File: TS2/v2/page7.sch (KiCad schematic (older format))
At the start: 9 parts, among them P1 FTDI (TERMINAL), P2 FTDI (HOST), U29 6850, U3 74LS00, U30 6850, U31 MC14411, U5 74LS04, Y1 1.842MHz

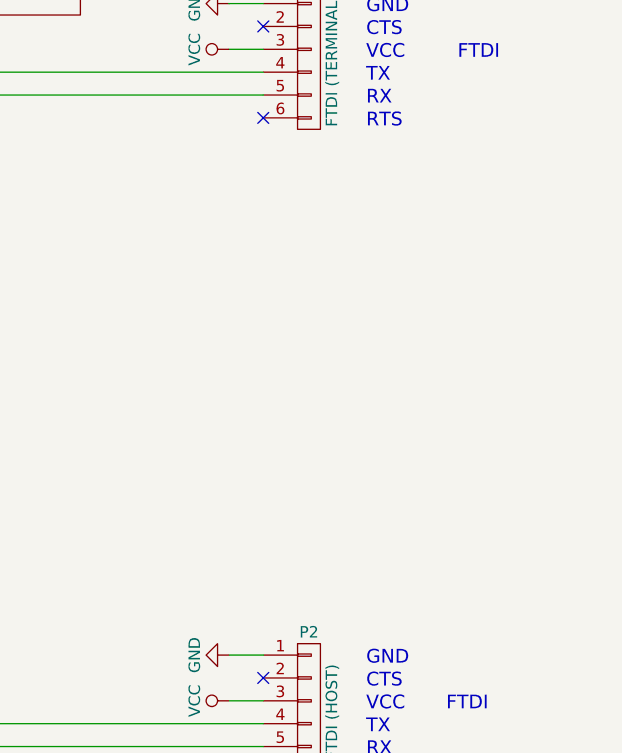
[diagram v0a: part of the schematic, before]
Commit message: Label serial ports.
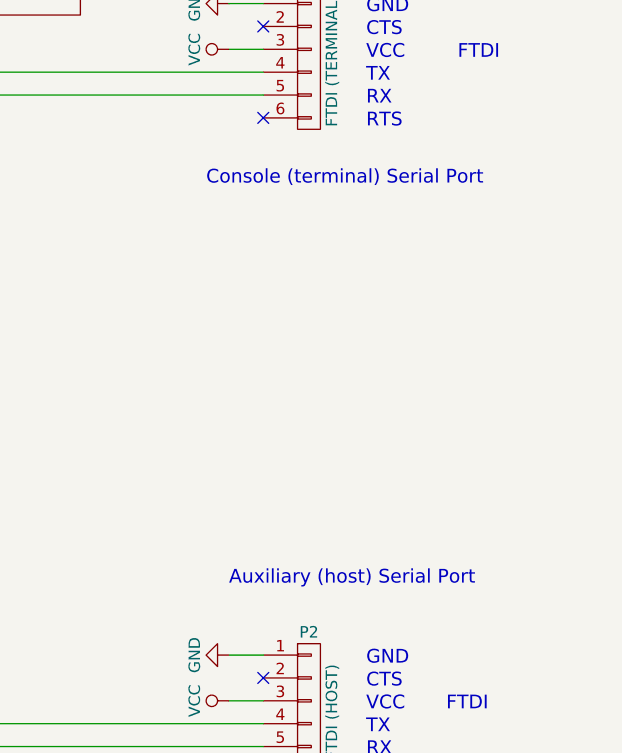
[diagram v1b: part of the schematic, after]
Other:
- note added: "Auxiliary (host) Serial Port"
- note added: "Console (terminal) Serial Port"
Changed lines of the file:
@@
 	2400 4050 2400 4250
 Connection ~ 2400 4150
+Text Notes 8450 4550 0    60   ~ 0
+Auxiliary (host) Serial Port
+Text Notes 8350 2800 0    60   ~ 0
+Console (terminal) Serial Port
 $EndSCHEMATC

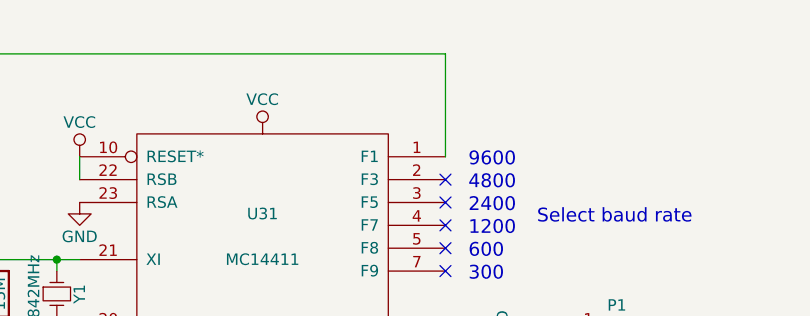
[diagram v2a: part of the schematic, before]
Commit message: List frequency of clock generator.
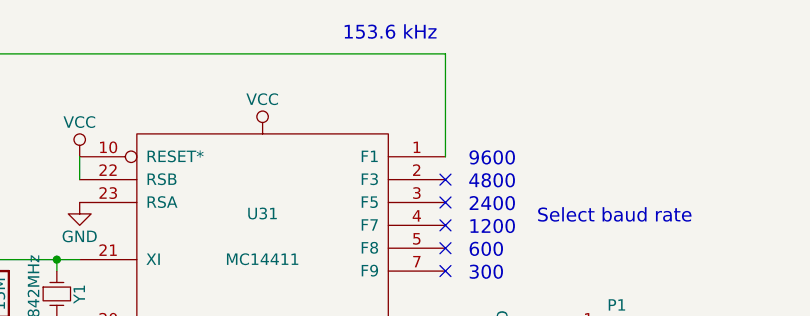
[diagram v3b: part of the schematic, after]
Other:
- note added: "153.6 kHz"
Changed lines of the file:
@@
 Text Notes 8350 2800 0    60   ~ 0
 Console (terminal) Serial Port
+Text Notes 7600 750  0    60   ~ 0
+153.6 kHz
 $EndSCHEMATC

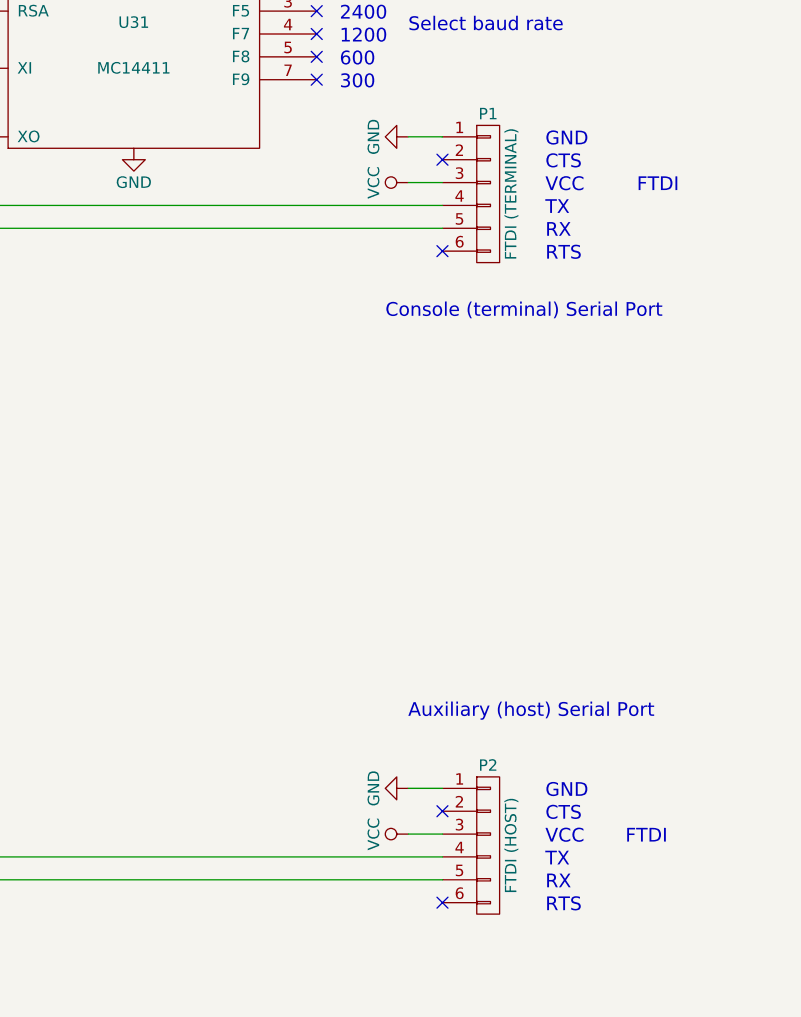
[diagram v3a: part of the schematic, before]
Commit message: Correction to FTDI connections.
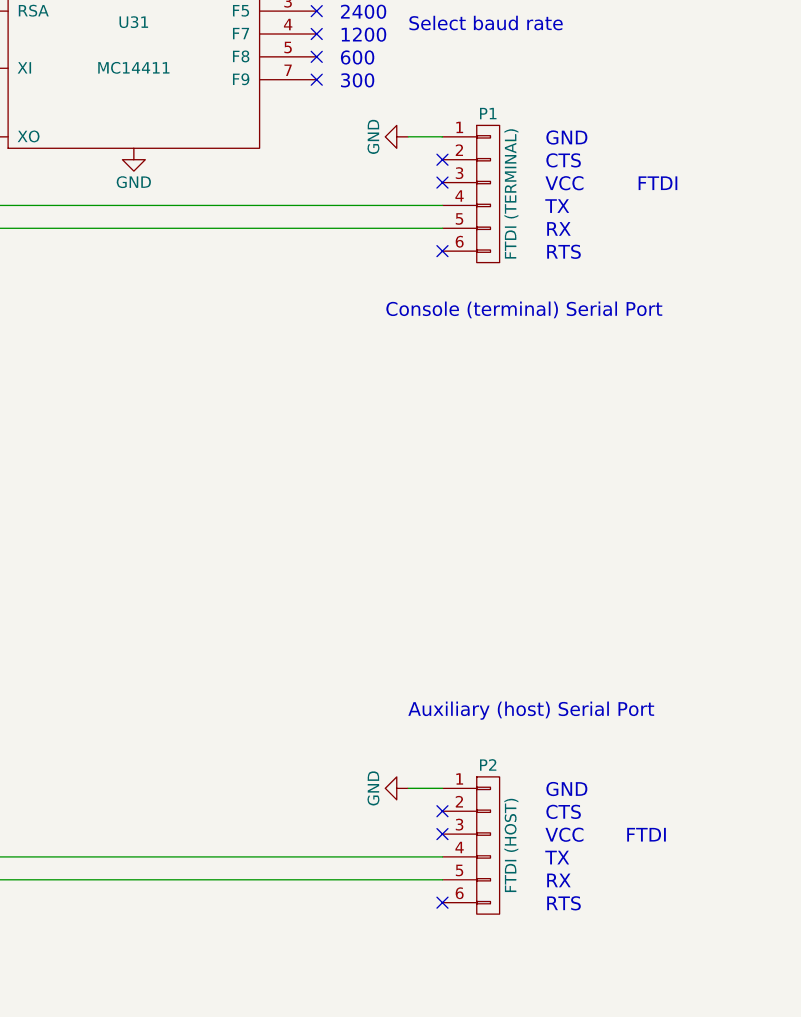
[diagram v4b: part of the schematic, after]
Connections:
- net VCC: no longer P1.3 (P3), P2.3 (P3)
- no-connect marks 11 -> 13
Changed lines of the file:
@@
 Sheet 8 9
 Title "TS2 68000 Single Board Computer"
-Date "2016-12-11"
+Date "2016-12-31"
 Rev "2.0"
 Comp "Jeff Tranter"
@@
 $EndComp
 $Comp
-L VCC #PWR096
-U 1 1 57CB20FE
-P 8450 2200
-F 0 "#PWR096" H 8450 2050 50  0001 C CNN
-F 1 "VCC" H 8450 2350 50  0000 C CNN
-F 2 "" H 8450 2200 50  0000 C CNN
-F 3 "" H 8450 2200 50  0000 C CNN
-	1    8450 2200
-	0    -1   -1   0
-$EndComp
-$Comp
 L GND #PWR097
 U 1 1 57CB2D6B
@@
 	1    8450 4850
 	0    1    1    0
-$EndComp
-$Comp
-L VCC #PWR099
-U 1 1 57CB3ACF
-P 8450 5050
-F 0 "#PWR099" H 8450 4900 50  0001 C CNN
-F 1 "VCC" H 8450 5200 50  0000 C CNN
-F 2 "" H 8450 5050 50  0000 C CNN
-F 3 "" H 8450 5050 50  0000 C CNN
-	1    8450 5050
-	0    -1   -1   0
 $EndComp
 $Comp
@@
 	8600 2000 8450 2000
 Wire Wire Line
-	8600 2200 8450 2200
-Wire Wire Line
 	4500 2300 8600 2300
 Wire Wire Line
@@
 Wire Wire Line
 	8450 4850 8600 4850
-Wire Wire Line
-	8600 5050 8450 5050
 Wire Wire Line
 	4500 5150 8600 5150
@@
 Text Notes 7600 750  0    60   ~ 0
 153.6 kHz
+NoConn ~ 8600 2200
+NoConn ~ 8600 5050
 $EndSCHEMATC

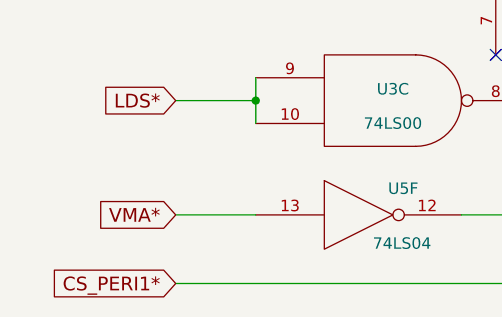
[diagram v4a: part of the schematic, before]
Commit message: Fixed error in original schematic. Prototype board is up and running.
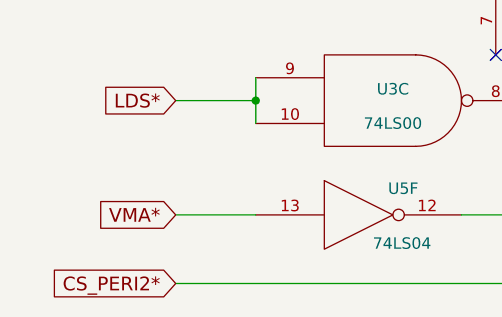
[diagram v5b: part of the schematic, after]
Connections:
- net CS_PERI1* renamed CS_PERI2*
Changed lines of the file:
@@
 Sheet 8 9
 Title "TS2 68000 Single Board Computer"
-Date "2016-12-31"
+Date "2017-01-03"
 Rev "2.0"
 Comp "Jeff Tranter"
@@
 $EndComp
 $Comp
-L GND #PWR087
+L GND #PWR089
 U 1 1 57C6835F
 P 7250 2050
-F 0 "#PWR087" H 7250 1800 50  0001 C CNN
+F 0 "#PWR089" H 7250 1800 50  0001 C CNN
 F 1 "GND" H 7250 1900 50  0000 C CNN
 F 2 "" H 7250 2050 50  0000 C CNN
@@
 $EndComp
 $Comp
-L VCC #PWR088
+L VCC #PWR090
 U 1 1 57C6838D
 P 7250 1150
-F 0 "#PWR088" H 7250 1000 50  0001 C CNN
+F 0 "#PWR090" H 7250 1000 50  0001 C CNN
 F 1 "VCC" H 7250 1300 50  0000 C CNN
 F 2 "" H 7250 1150 50  0000 C CNN
@@
 $EndComp
 $Comp
-L GND #PWR089
+L GND #PWR091
 U 1 1 57C688B5
 P 6450 1450
-F 0 "#PWR089" H 6450 1200 50  0001 C CNN
+F 0 "#PWR091" H 6450 1200 50  0001 C CNN
 F 1 "GND" H 6450 1300 50  0000 C CNN
 F 2 "" H 6450 1450 50  0000 C CNN
@@
 $EndComp
 $Comp
-L VCC #PWR090
+L VCC #PWR092
 U 1 1 57C688E3
 P 6450 1250
-F 0 "#PWR090" H 6450 1100 50  0001 C CNN
+F 0 "#PWR092" H 6450 1100 50  0001 C CNN
 F 1 "VCC" H 6450 1400 50  0000 C CNN
 F 2 "" H 6450 1250 50  0000 C CNN
@@
 VMA*
 Text GLabel 2050 7700 0    60   Input ~ 0
-CS_PERI1*
+CS_PERI2*
 Text GLabel 2100 4150 0    60   Input ~ 0
 UDS*
@@
 D15
 $Comp
-L VCC #PWR091
+L VCC #PWR093
 U 1 1 57C7A398
 P 3800 1650
-F 0 "#PWR091" H 3800 1500 50  0001 C CNN
+F 0 "#PWR093" H 3800 1500 50  0001 C CNN
 F 1 "VCC" H 3800 1800 50  0000 C CNN
 F 2 "" H 3800 1650 50  0000 C CNN
@@
 $EndComp
 $Comp
-L GND #PWR092
+L GND #PWR094
 U 1 1 57C7A4BC
 P 3800 3550
-F 0 "#PWR092" H 3800 3300 50  0001 C CNN
+F 0 "#PWR094" H 3800 3300 50  0001 C CNN
 F 1 "GND" H 3800 3400 50  0000 C CNN
 F 2 "" H 3800 3550 50  0000 C CNN
@@
 $EndComp
 $Comp
-L VCC #PWR093
+L VCC #PWR095
 U 1 1 57C7A5E0
 P 3800 4500
-F 0 "#PWR093" H 3800 4350 50  0001 C CNN
+F 0 "#PWR095" H 3800 4350 50  0001 C CNN
 F 1 "VCC" H 3800 4650 50  0000 C CNN
 F 2 "" H 3800 4500 50  0000 C CNN
@@
 $EndComp
 $Comp
-L GND #PWR094
+L GND #PWR096
 U 1 1 57C7A616
 P 3800 6400
-F 0 "#PWR094" H 3800 6150 50  0001 C CNN
+F 0 "#PWR096" H 3800 6150 50  0001 C CNN
 F 1 "GND" H 3800 6250 50  0000 C CNN
 F 2 "" H 3800 6400 50  0000 C CNN
@@
 $EndComp
 $Comp
-L GND #PWR095
+L GND #PWR097
 U 1 1 57CB2088
 P 8450 2000
-F 0 "#PWR095" H 8450 1750 50  0001 C CNN
+F 0 "#PWR097" H 8450 1750 50  0001 C CNN
 F 1 "GND" H 8450 1850 50  0000 C CNN
 F 2 "" H 8450 2000 50  0000 C CNN
@@
 $EndComp
 $Comp
-L GND #PWR097
+L GND #PWR098
 U 1 1 57CB2D6B
 P 4500 3000
-F 0 "#PWR097" H 4500 2750 50  0001 C CNN
+F 0 "#PWR098" H 4500 2750 50  0001 C CNN
 F 1 "GND" H 4500 2850 50  0000 C CNN
 F 2 "" H 4500 3000 50  0000 C CNN
@@
 $EndComp
 $Comp
-L GND #PWR098
+L GND #PWR099
 U 1 1 57CB394C
 P 8450 4850
-F 0 "#PWR098" H 8450 4600 50  0001 C CNN
+F 0 "#PWR099" H 8450 4600 50  0001 C CNN
 F 1 "GND" H 8450 4700 50  0000 C CNN
 F 2 "" H 8450 4850 50  0000 C CNN

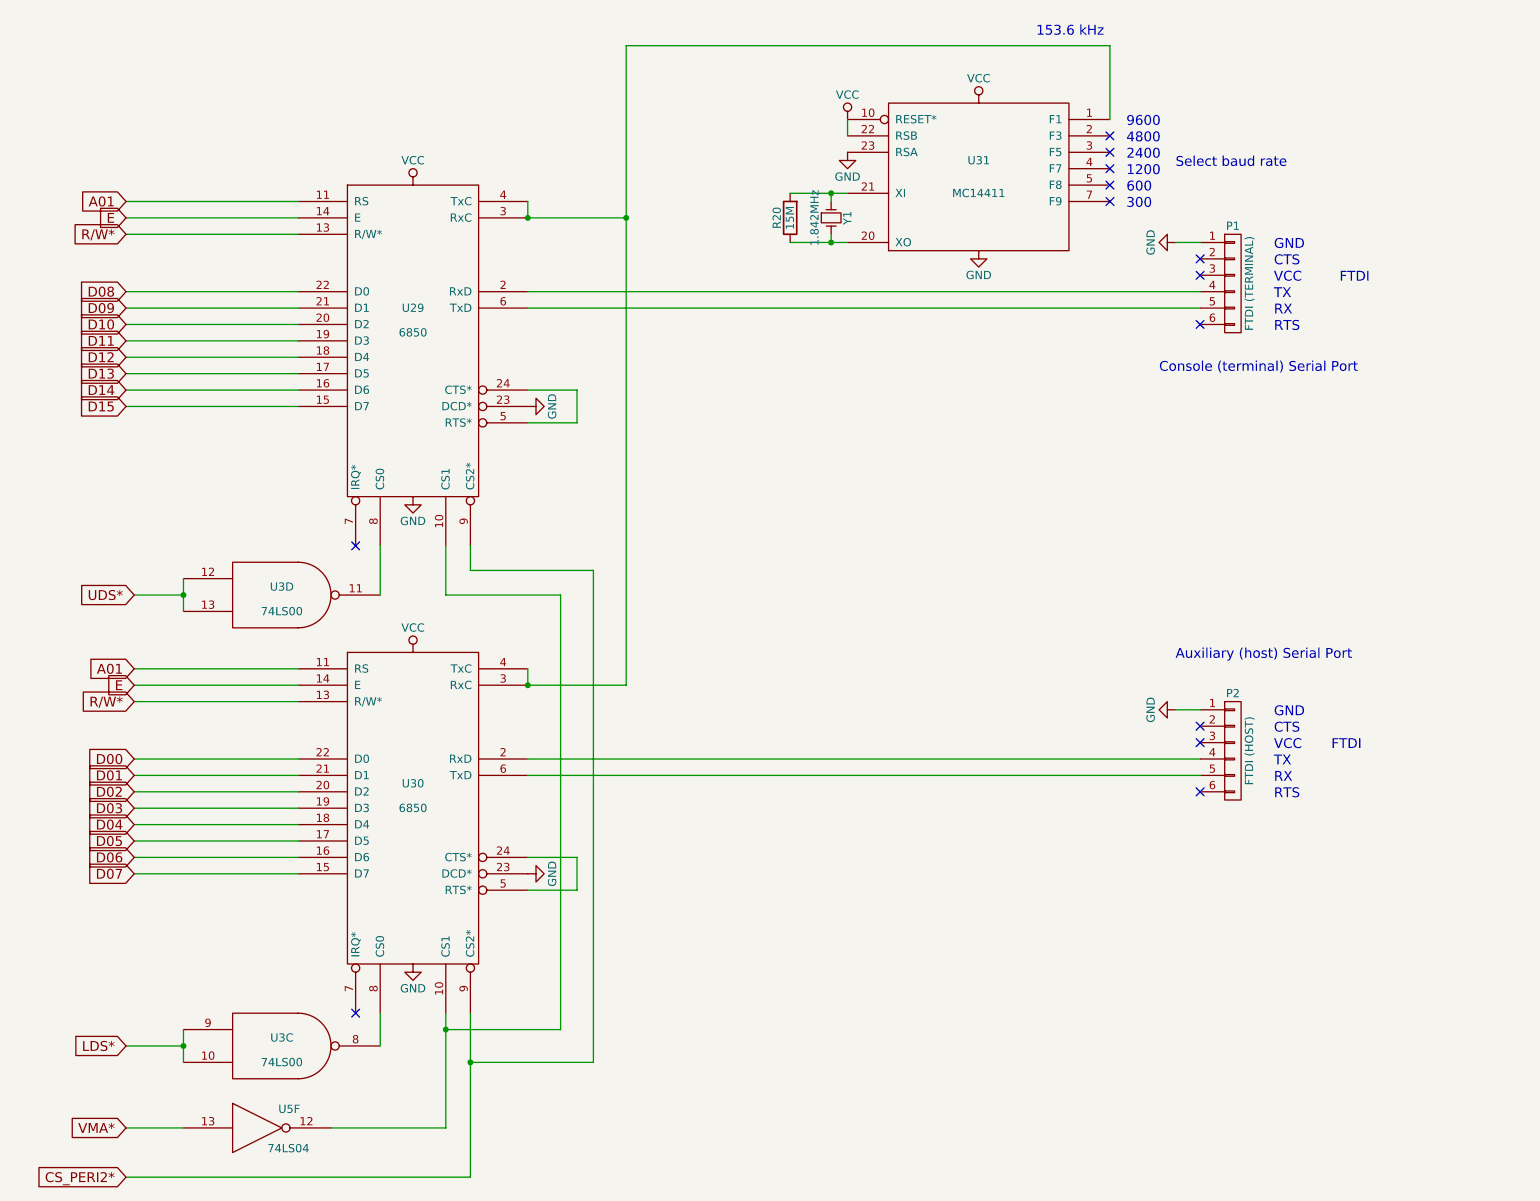
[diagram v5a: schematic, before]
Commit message: Add some notes on serial port page.
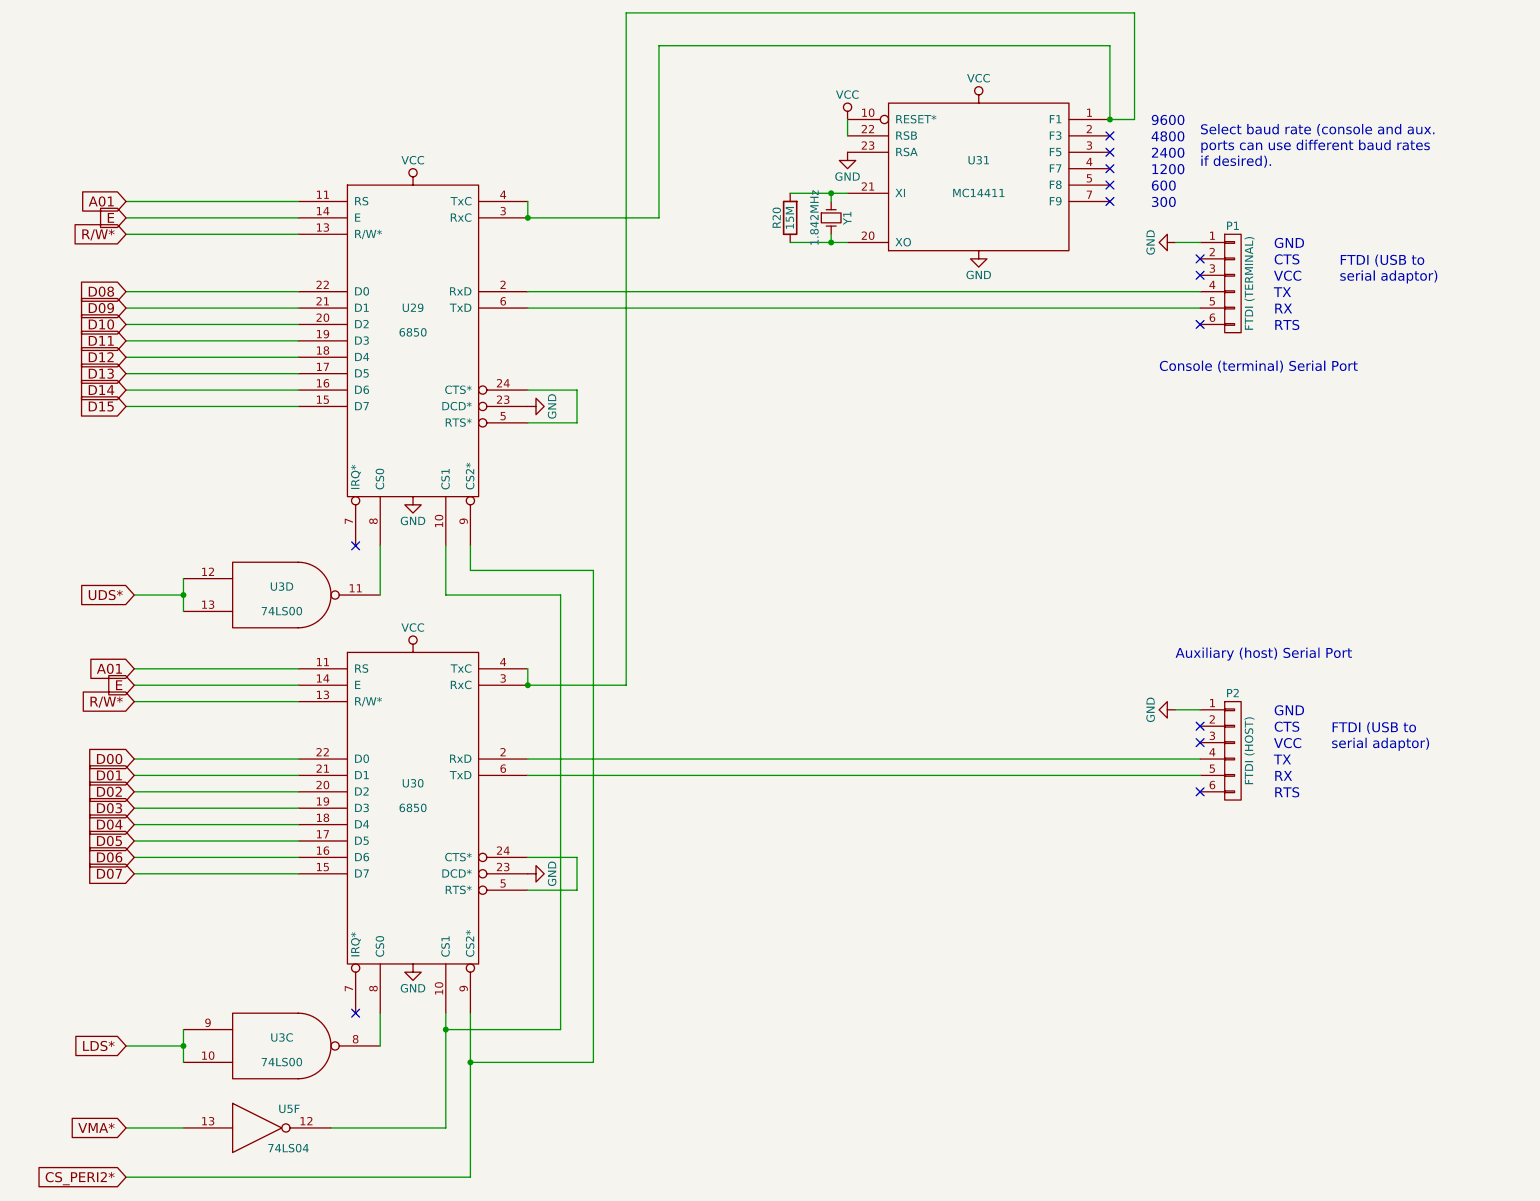
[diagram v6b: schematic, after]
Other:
- note added: "FTDI (USB to\nserial adaptor)"
- note added: "Select baud rate (console and aux.\nports can use different baud rates\nif desired)."
- note removed: "153.6 kHz"
- note removed: "FTDI"
- note removed: "Select baud rate"
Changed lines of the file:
@@
 Sheet 8 9
 Title "TS2 68000 Single Board Computer"
-Date "2017-01-03"
+Date "2017-01-05"
 Rev "2.0"
 Comp "Jeff Tranter"
@@
 NoConn ~ 8600 5350
 NoConn ~ 8600 4950
-Text Notes 8150 1300 0    60   ~ 0
+Text Notes 8300 1300 0    60   ~ 0
 9600
-Text Notes 8150 1400 0    60   ~ 0
+Text Notes 8300 1400 0    60   ~ 0
 4800
-Text Notes 8150 1500 0    60   ~ 0
+Text Notes 8300 1500 0    60   ~ 0
 2400
-Text Notes 8150 1600 0    60   ~ 0
+Text Notes 8300 1600 0    60   ~ 0
 1200
-Text Notes 8150 1700 0    60   ~ 0
+Text Notes 8300 1700 0    60   ~ 0
 600
-Text Notes 8150 1800 0    60   ~ 0
+Text Notes 8300 1800 0    60   ~ 0
 300
-Text Notes 8450 1550 0    60   ~ 0
-Select baud rate
+Text Notes 8600 1550 0    60   ~ 0
+Select baud rate (console and aux.\nports can use different baud rates\nif desired).
 Wire Wire Line
 	6100 1700 6450 1700
@@
 	3100 1750 2050 1750
 Wire Wire Line
-	8050 1250 8050 1250
+	8050 1250 8200 1250
 Wire Wire Line
 	8050 1250 8050 800
@@
 	5100 4700 4500 4700
 Wire Wire Line
-	5100 800  5100 4700
-Connection ~ 5100 1850
-Wire Wire Line
-	4500 1850 5100 1850
+	4500 1850 5300 1850
 Connection ~ 4500 4700
 Wire Wire Line
 	4500 4700 4500 4600
 Wire Wire Line
-	8050 800  5100 800
+	8050 800  5300 800
 Text Notes 9450 2250 0    60   ~ 0
-FTDI
+FTDI (USB to\nserial adaptor)
 Text Notes 9400 5100 0    60   ~ 0
-FTDI
+FTDI (USB to\nserial adaptor)
 $Comp
 L 74LS00 U3
@@
 Connection ~ 2400 6900
 Wire Wire Line
-	4000 7400 4000 6700
-Wire Wire Line
-	3300 7400 4000 7400
+	4000 6700 4000 7400
+Wire Wire Line
+	4000 7400 3300 7400
 Wire Wire Line
 	2400 7400 2050 7400
@@
 Text Notes 8350 2800 0    60   ~ 0
 Console (terminal) Serial Port
-Text Notes 7600 750  0    60   ~ 0
-153.6 kHz
 NoConn ~ 8600 2200
 NoConn ~ 8600 5050
+Wire Wire Line
+	5300 800  5300 1850
+Wire Wire Line
+	5100 4700 5100 600
+Wire Wire Line
+	5100 600  8200 600
+Wire Wire Line
+	8200 600  8200 1250
+Connection ~ 8050 1250
 $EndSCHEMATC
